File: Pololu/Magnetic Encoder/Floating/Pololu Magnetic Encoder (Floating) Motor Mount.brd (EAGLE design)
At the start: 15.2 x 15.2 mm, 6 parts

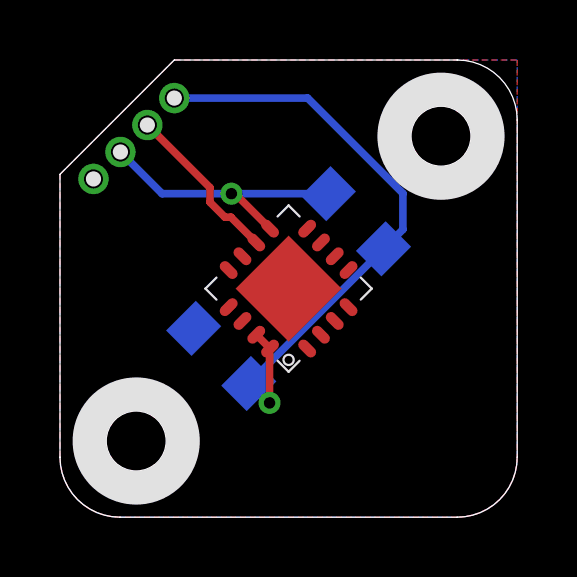
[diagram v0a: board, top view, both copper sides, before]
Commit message: Removed projects that I'm unlikely to ever get to again.
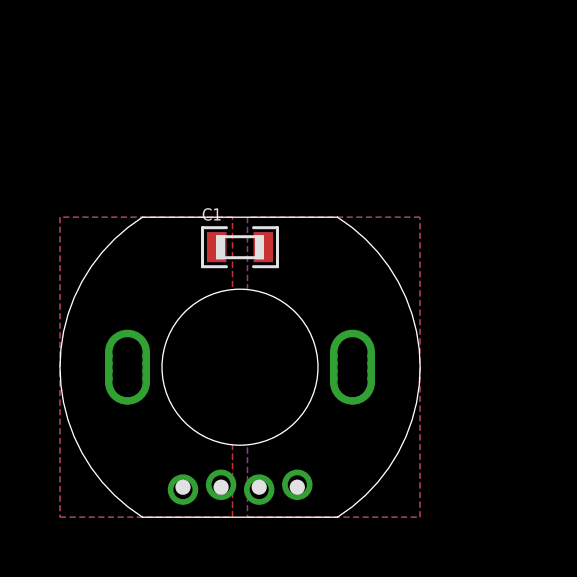
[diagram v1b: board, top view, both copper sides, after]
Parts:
- removed R1: 47k, .standardparts:0805
- removed U$2: G2X[1/5]2---RSA16, TI_MSP430_v16:RSA16
- removed U$5: 1X4, .headers(.5in):1X4
- removed U$7, U$8: HOLE.2MM, .stdscrewholes:2MM
- added U$1: 1X4.LOCK, headers(.05in):1X4.LOCK
- C1: value 1uF -> .1uF; device .standardparts:0805 -> standardparts:0603
- moved C1 3.68 mm to (6.00, 9.00), flipped to the top, turned to 0 degrees
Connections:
- removed net 3.3V: C1.1, R1.1, U$2.15, U$2.16, U$5.1
- removed net GND: C1.2, U$2.13, U$2.14, U$5.4
- removed net SBWTCK: U$2.10, U$5.2
- removed net SBWTDIO: R1.2, U$2.9, U$5.3
- new net M+: C1.1, U$1.1, U$1.2
- new net M-: C1.2, U$1.3, U$1.4
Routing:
- net 3.3V: track 20.8 -> 0.00 mm, vias 1 -> 0
- net SBWTDIO: track 9.28 -> 0.00 mm, vias 1 -> 0
- net SBWTCK: track 5.53 -> 0.00 mm
- added copper zone on layer 1, net M+
- added copper zone on layer 16, net M+
- added copper zone on layer 1, net M-
- added copper zone on layer 16, net M-
- removed copper zone on layer 1, net GND
- removed copper zone on layer 16, net GND
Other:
- board size 15.2 x 15.2 mm -> 12 x 10 mm
- board text added: "+"
- board text added: "-"
- board text removed: "3.6v"
- board text removed: "Cruz Monrreal II"
- board text removed: "GND"
- board text removed: "MSP430 QFP16 PGMR"
- board text removed: "SBWTCK"
- board text removed: "SBWTDIO"
